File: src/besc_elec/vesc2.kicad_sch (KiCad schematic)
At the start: 56 parts, among them J101 XT-30-TOP, J102 HALL/ENCODER, J103 SM02B-PASS, J104 IDC6, J105 MR_60_TOP, U101 STM32G474_VESC, U102 TCAN1462V, U103 HX4002, Y101 24Mhz

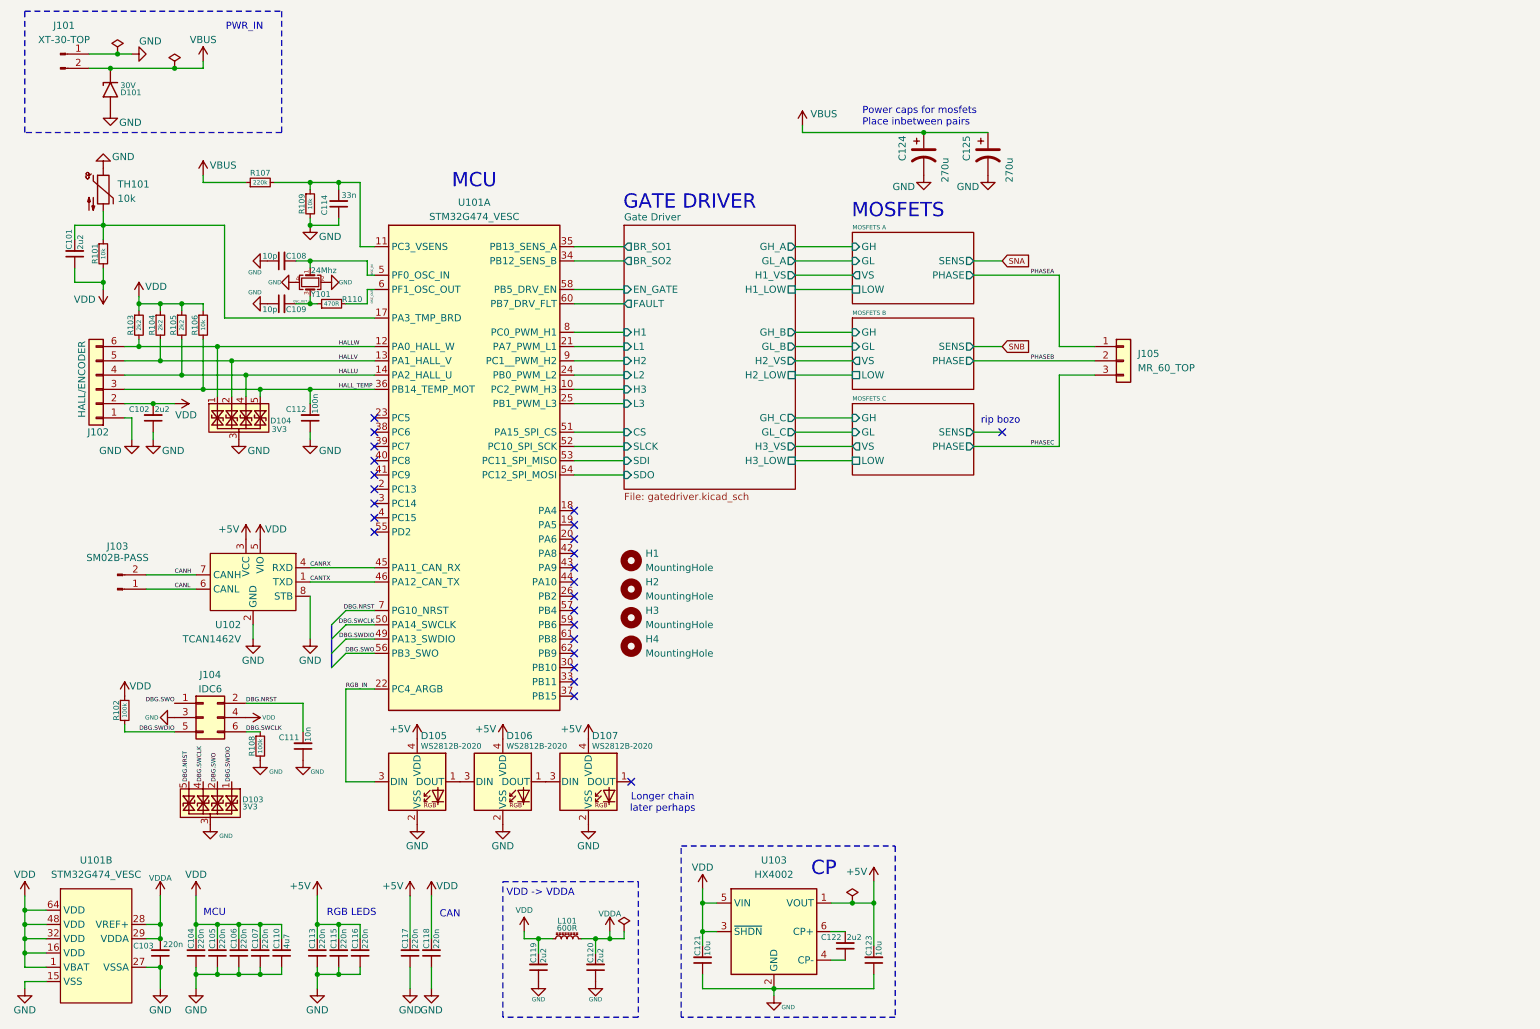
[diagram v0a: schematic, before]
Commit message: added DRV8323HRTAR symbol and footprint
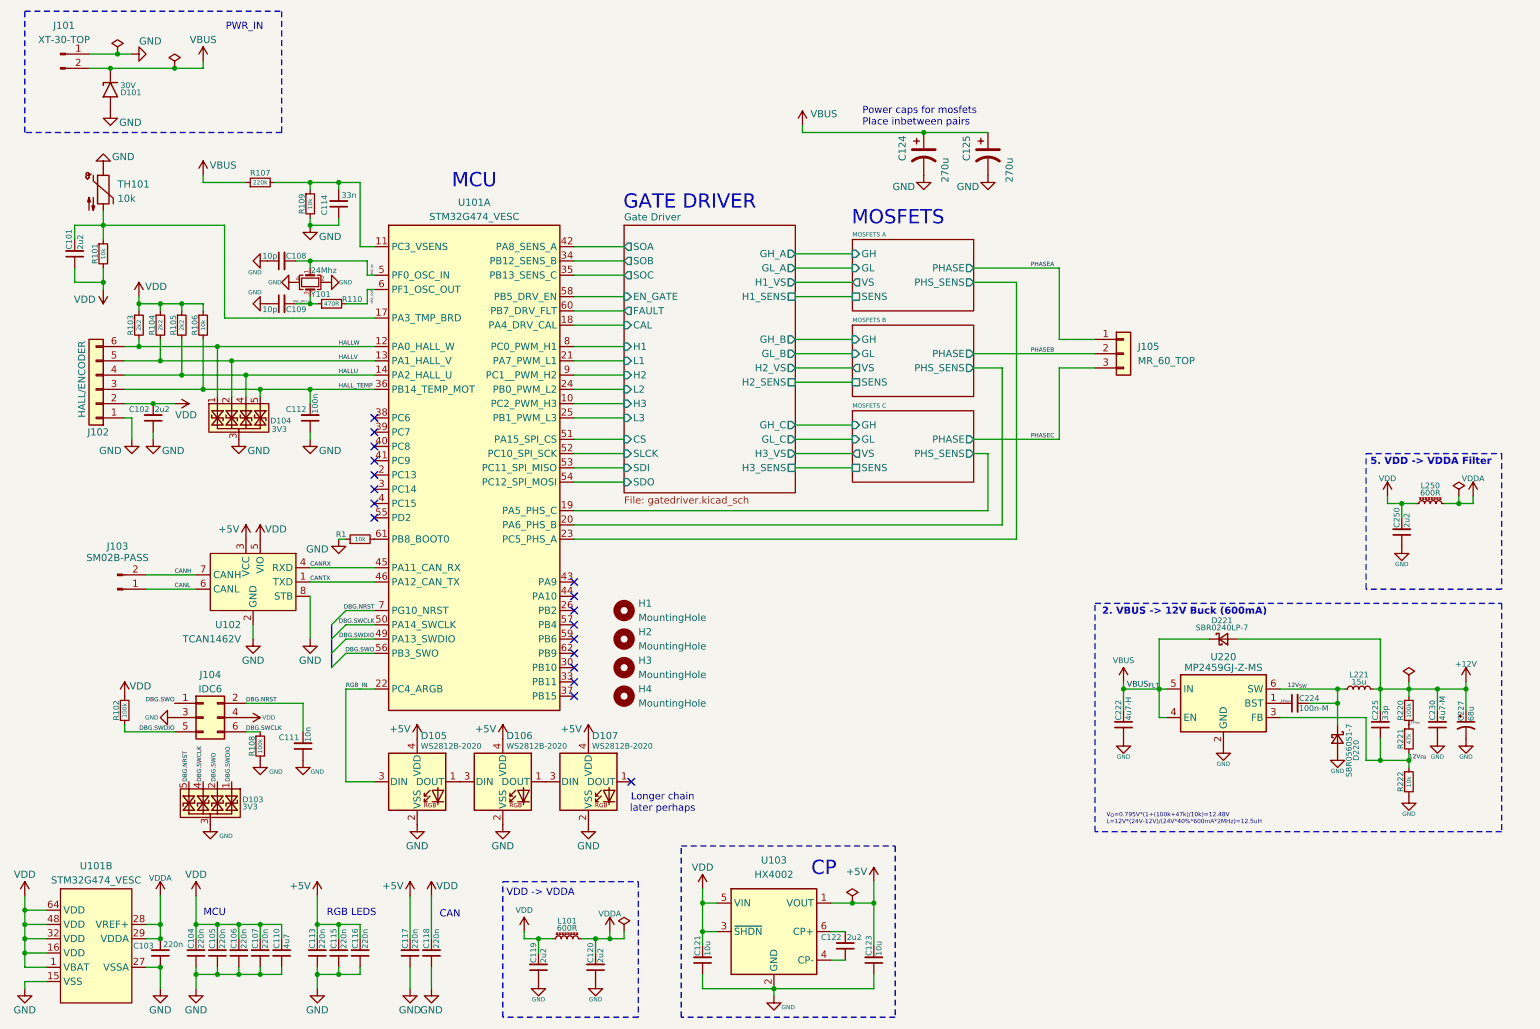
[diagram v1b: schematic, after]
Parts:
- added C222: 4u7-H, Capacitor_SMD:C_1210_3225Metric, symbol Bluesat:C_CompactV
- added C224: 100n-M, Capacitor_SMD:C_0402_1005Metric, symbol Bluesat:C_CompactV
- added C225: 33p, Capacitor_SMD:C_0402_1005Metric, symbol Bluesat:C_CompactV
- added C227: 68u, Capacitor_SMD:CP_Elec_6.3x7.7, symbol Device:C_Polarized_Small_US
- added C230: 4u7-M, Capacitor_SMD:C_1206_3216Metric, symbol Bluesat:C_CompactV
- added C250: 2u2, Capacitor_SMD:C_0603_1608Metric, symbol Bluesat:C_CompactV
- added D220: SBR0560S1-7, Diode_SMD:D_SOD-123, symbol Device:D_Schottky_Small
- added D221: SBR0240LP-7, Diode_SMD:D_SOD-882, symbol Device:D_Schottky_Small
- added L221: 15u, Inductor_SMD:L_Changjiang_FNR5040S, symbol Device:L_Small
- added L250: 600R, Resistor_SMD:R_0402_1005Metric, symbol Device:L_Ferrite_Small
- added R1: 10k, symbol Bluesat:R_CompactH
- added R220: 100k, Resistor_SMD:R_0402_1005Metric, symbol Bluesat:R_CompactV
- added R221: 47k, Resistor_SMD:R_0402_1005Metric, symbol Bluesat:R_CompactV
- added R222: 10k, Resistor_SMD:R_0402_1005Metric, symbol Bluesat:R_CompactV
- added U220: MP2459GJ-Z-MS, Package_TO_SOT_SMD:TSOT-23-6, symbol Bluesat:MP2459GJ-Z-MS
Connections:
- net GND: now also C222.1, C227.2, C230.1, C250.1, D220.2 (A), R1.1, R222.2, U220.2 (GND)
- net VBUS: now also C222.2, D221.1 (K), U220.4 (EN), U220.5 (IN)
- net VDD: now also C250.2, L250.1
- net VDDA: now also L250.2
- net Gate Driver/CAL: now reaches U101.18 (PA4_DRV_CAL)
- net MOSFETS C/PHS_SENS: now reaches U101.19 (PA5_PHS_C)
- net MOSFETS B/PHS_SENS: now reaches U101.20 (PA6_PHS_B)
- net MOSFETS A/PHS_SENS: now reaches U101.23 (PC5_PHS_A)
- net Gate Driver/SOA: now reaches U101.42 (PA8_SENS_A)
- net at U101.61 (PB8_BOOT0): now also R1.2
- net Gate Driver/BR_SO1 renamed Gate Driver/SOC
- net Gate Driver/BR_SO2 renamed Gate Driver/SOB
- new net +12V: C225.2, C227.1, C230.2, D221.2 (A), L221.2, R220.1
- new net 12V_{BST}: C224.1, U220.1 (BST)
- new net 12V_{FBM}: R220.2, R221.1
- new net 12V_{FB}: C225.1, R221.2, R222.1, U220.3 (FB)
- new net 12V_{SW}: C224.2, D220.1 (K), L221.1, U220.6 (SW)
- no-connect marks 25 -> 18
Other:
- sheet Gate Driver ports: added CAL, H1_SENS, H2_SENS, H3_SENS, SOA, SOB, SOC; removed BR_SO1, BR_SO2, H1_LOW, H2_LOW, H3_LOW
- sheet MOSFETS A ports: added PHS_SENS; removed LOW
- sheet MOSFETS B ports: added PHS_SENS; removed LOW
- sheet MOSFETS C ports: added PHS_SENS; removed LOW
- note added: "2. VBUS -> 12V Buck (600mA)"
- note added: "5. VDD -> VDDA Filter"
- note added: "V_{O}=0.795V*(1+(100k+47k)/10k)=12.48Vr L=12V*(24V-12V)/(24V*40%*600mA*2MHz)=12.5uH"
- note removed: "rip bozo"
- moved on the sheet: H1, H2, H3, H4, J105

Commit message: switched gate driver variant from RS->HR
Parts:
- added R115, R116: 4k7, symbol Bluesat:R_CompactV
- renumbered C222 to C126, C224 to C127, C225 to C128, C230 to C129, C227 to C130, C250 to C131, L221 to L102, L250 to L103, R108 to R103, R103 to R104, R104 to R105, R105 to R106, R106 to R107, R107 to R108, R1 to R111, R222 to R112, R221 to R113, R220 to R114, U220 to U104
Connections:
- net VDD: now also R115.1, R116.1
- net at U101.40 (PC8_I2C_SCL): now also R115.2
- net at U101.41 (PC9_I2C_SDA): now also R116.2
- net Gate Driver/CS: no longer names the net of U101.51 (PA15_SPI_CS)
- net Gate Driver/SDI: no longer names the net of U101.53 (PC11_SPI_MISO)
- net Gate Driver/SDO: no longer names the net of U101.54 (PC12_SPI_MOSI)
- net Gate Driver/SLCK: no longer names the net of U101.52 (PC10_SPI_SCK)
- no-connect marks 18 -> 16
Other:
- sheet Gate Driver ports: added none; removed CS, SDI, SDO, SLCK
- note added: "(stolen)"
- note added: "Buck"
- moved on the sheet: C124, C125, H1, H2, H3, H4, J105
